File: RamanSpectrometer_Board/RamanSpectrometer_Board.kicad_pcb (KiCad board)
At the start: 2 copper layers, 49.3 x 90.9 mm, 33 parts, among them J1 RJ45_LED_Shielded, Q1 BSS138, Q2 BSS138, Q3 BSS138, Q4 BSS138, Q5 BSS138, U1 Teensy4.1_DEV-16771, U2 OKI 12V-5V, U3 OKI 5V-3V

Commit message: PCB Raman updates
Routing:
- net GND: vias 66 -> 31
- net +12V: vias 0 -> 14

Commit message: PCB Raman again
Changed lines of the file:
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@@
 		(net 4)
 		(net_name "+12V")
-		(layer "F.Cu")
+		(layers "F&B.Cu")
 		(hatch edge 0.5)
 		(priority 2)
-		(connect_pads
+		(connect_pads yes
 			(clearance 0.5)
 		)
 		(min_thickness 0.25)
 		(filled_areas_thickness no)
-		(fill yes
+		(fill
 			(thermal_gap 0.5)
 			(thermal_bridge_width 0.5)
@@
 		(polygon
 			(pts
-				(xy 143.667 53.084) (xy 164.495 53.084) (xy 164.495 123.696) (xy 143.667 123.696)
+				(xy 148.59 53.086) (xy 164.592 53.084) (xy 164.592 123.696) (xy 148.59 123.698)
 			)
 		)
@@
 		(polygon
 			(pts
-				(xy 142.905 43.432) (xy 192.181 43.432) (xy 192.181 134.364) (xy 142.905 134.364)
+				(xy 142.875 43.432) (xy 192.151 43.432) (xy 192.151 134.364) (xy 142.875 134.364)
 			)
 		)
-	)
-	(zone
-		(net 4)
-		(net_name "+12V")
-		(layer "B.Cu")
-		(hatch edge 0.5)
-		(priority 3)
-		(connect_pads
-			(clearance 0.5)
-		)
-		(min_thickness 0.25)
-		(filled_areas_thickness no)
-		(fill yes
-			(thermal_gap 0.5)
-			(thermal_bridge_width 0.5)
-		)
-		(polygon
-			(pts
-				(xy 143.667 53.084) (xy 164.495 53.084) (xy 164.495 123.696) (xy 143.667 123.696)
-			)
-		)
-	)
-	(zone
-		(net 2)
-		(net_name "GND")
-		(layer "B.Cu")
-		(hatch edge 0.5)
-		(priority 1)
-		(connect_pads
-			(clearance 0.5)
-		)
-		(min_thickness 0.25)
-		(filled_areas_thickness no)
-		(fill yes
-			(thermal_gap 0.5)
-			(thermal_bridge_width 0.5)
-		)
-		(polygon
-			(pts
-				(xy 142.905 43.432) (xy 192.181 43.432) (xy 192.181 134.364) (xy 142.905 134.364)
-			)
-		)

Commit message: PCB Raman 12V Plane
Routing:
- removed copper zone on B.Cu, net +12V
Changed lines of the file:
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@@
 		(at 174.244 102.108 90)
 		(property "Reference" "U1"
-			(at 7.108 -4.244 -90)
+			(at -30.48 0 0)
 			(layer "F.SilkS")
 			(effects
@@
 	)
 	(via
-		(at 157.48 106.68)
+		(at 157.48 91.44)
 		(size 0.6)
 		(drill 0.3)
@@
 	)
 	(via
-		(at 157.48 91.44)
+		(at 152.4 81.28)
 		(size 0.6)
 		(drill 0.3)
@@
 	)
 	(via
-		(at 152.4 81.28)
+		(at 152.4 101.6)
 		(size 0.6)
 		(drill 0.3)
@@
 	)
 	(via
-		(at 152.4 101.6)
+		(at 152.4 86.36)
 		(size 0.6)
 		(drill 0.3)
@@
 	)
 	(via
-		(at 152.4 86.36)
+		(at 157.48 106.68)
 		(size 0.6)
 		(drill 0.3)
@@
 		(net 4)
 		(net_name "+12V")
-		(layers "F&B.Cu")
+		(layer "F.Cu")
 		(hatch edge 0.5)
 		(priority 2)
@@
 		(min_thickness 0.25)
 		(filled_areas_thickness no)
-		(fill
+		(fill yes
 			(thermal_gap 0.5)
 			(thermal_bridge_width 0.5)

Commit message: PCB Raman edit and TOF
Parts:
- moved C1 0.35 mm to (168.9, 67.5)
- renumbered D1 to 12V, D3 to 3.3V, D2 to 5V
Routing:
- net +12V: track 0.00 -> 95.0 mm, vias 14 -> 1
- net Red_LED: track 78.0 -> 85.6 mm
- net Green_LED: track 82.7 -> 88.2 mm
- net +3.3V: track 58.2 -> 59.6 mm
- net +3V3: track 24.7 -> 25.8 mm
- net Diode Control: track 87.3 -> 86.3 mm
- net +5V: track 124.1 -> 123.2 mm
- net Net-(C1-Pad1): track 12.8 -> 13.6 mm
- net CCD_ROG_5V: track 11.0 -> 11.6 mm
- net R-: track 68.4 -> 67.9 mm
- net GND: vias 31 -> 39
- removed copper zone on F.Cu, net +12V

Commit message: ihateyoujesse
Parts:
- removed 12V, 3.3V, 5V: Green, LED_SMD:LED_0603_1608Metric_Pad1.05x0.95mm_HandSolder
- removed Q3, Q4: BSS138, Package_TO_SOT_SMD:SOT-23
- removed R10: 33, Resistor_SMD:R_0603_1608Metric_Pad0.98x0.95mm_HandSolder
- removed R8: 78.7, Resistor_SMD:R_0603_1608Metric_Pad0.98x0.95mm_HandSolder
- added D1: Green, LED_SMD:LED_0603_1608Metric_Pad1.05x0.95mm_HandSolder, F.Cu at (150.5, 113.8)
- added D2: Green, LED_SMD:LED_0603_1608Metric_Pad1.05x0.95mm_HandSolder, F.Cu at (150.5, 118.1)
- added D3: Green, LED_SMD:LED_0603_1608Metric_Pad1.05x0.95mm_HandSolder, F.Cu at (150.5, 122.4)
- added U4: VL53L4CX, VL53L4CX:VL53L4CX, F.Cu at (202.7, 94.5)
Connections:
- U1 pad 17: unconnected-(U1-A3-Pad17) -> GPIO
- U1 pad 18: unconnected-(U1-A4-Pad18) -> SDA
- U1 pad 19: unconnected-(U1-A5-Pad19) -> SCL
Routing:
- net Green_LED: track 88.2 -> 0.00 mm
- net Red_LED: track 85.6 -> 0.00 mm
- net +12V: track 95.0 -> 57.2 mm, vias 1 -> 2
- net SDA: vias 0 -> 1
- net GND: vias 39 -> 34

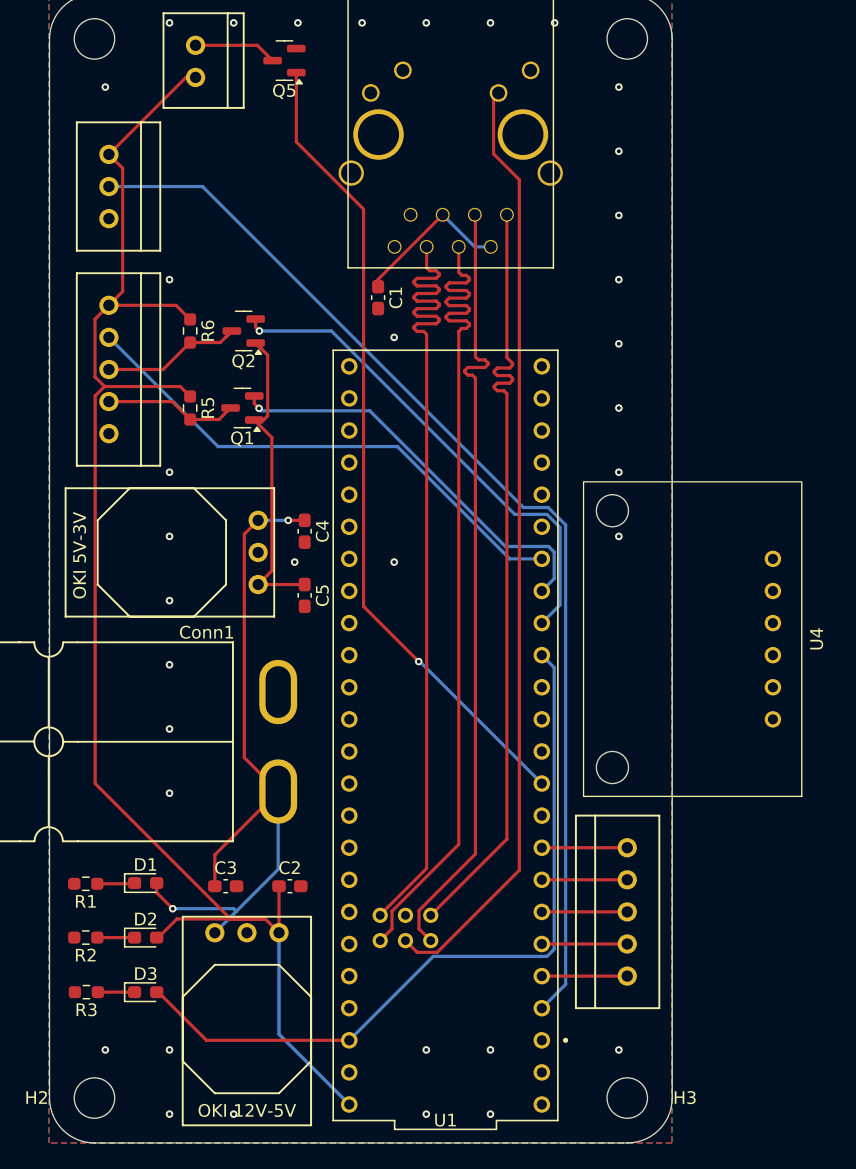
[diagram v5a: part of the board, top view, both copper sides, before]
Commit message: Raman PCB Additions
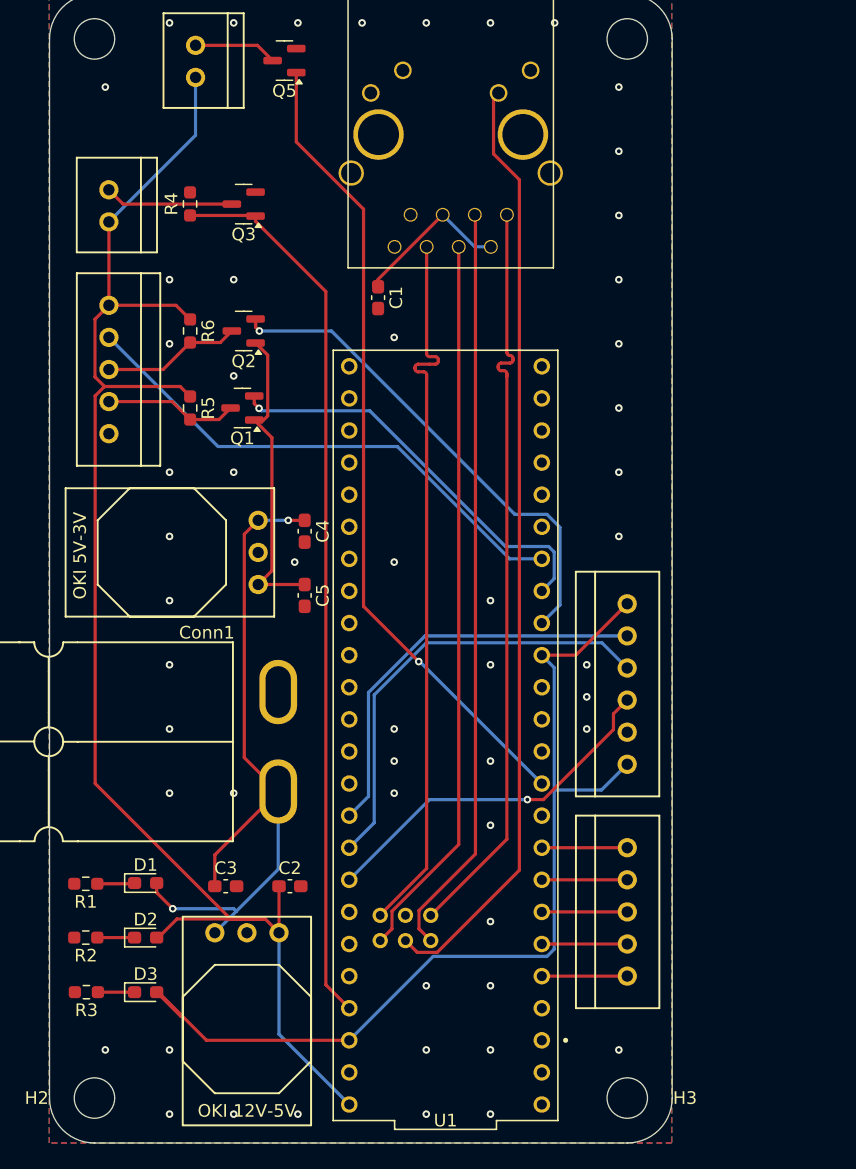
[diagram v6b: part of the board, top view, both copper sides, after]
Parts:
- removed Conn3: Diode, MRDT_Connectors:MOLEX_SL_03_Vertical
- removed U4: VL53L4CX, VL53L4CX:VL53L4CX
- added Conn6: Laser, MRDT_Connectors:MOLEX_SL_02_Vertical, F.Cu at (147.6, 58.9)
- added Conn7: TOF Sensor, MRDT_Connectors:MOLEX_SL_06_Vertical, F.Cu at (192.6, 98.2)
- added Q3: BSS138, Package_TO_SOT_SMD:SOT-23, F.Cu at (158.3, 60.1)
- added R4: 4.7k, Resistor_SMD:R_0603_1608Metric_Pad0.98x0.95mm_HandSolder, F.Cu at (154.0, 60.0)
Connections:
- U1 pad 23: unconnected-(U1-A9-Pad23) -> Green_Laser_3V3
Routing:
- net Diode Control: track 86.3 -> 0.00 mm
- net Green_Laser_3V3: track 0.00 -> 71.0 mm
- net SDA: track 0.00 -> 35.7 mm, vias 1 -> 0
- net GPIO: track 0.00 -> 32.7 mm
- net SCL: track 0.00 -> 28.6 mm, vias 0 -> 1
- net +3.3V: track 59.6 -> 77.5 mm
- net R+: track 68.0 -> 57.5 mm
- net R-: track 67.9 -> 57.4 mm
- net Net-(Q3-D): track 0.00 -> 10.2 mm
- net T-: track 62.6 -> 59.7 mm
- net T+: track 62.4 -> 59.6 mm
- net +12V: track 57.2 -> 59.1 mm
- net +5V: track 123.2 -> 122.0 mm
- net +3V3: track 25.8 -> 25.1 mm
- net CCD_ROG_5V: track 11.6 -> 11.0 mm
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
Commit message: Raman PCB Final
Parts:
- added G***: LOGO, MRDT_Silkscreens:0_MRDT_Logo_7.5mm, F.Cu at (187.7, 74.2)
- added G***: LOGO, LOGO, F.Cu at (188.5, 82.7)
- added G***: LOGO, LOGO, B.Cu at (168.7, 88.9)
- renumbered D1 to 12V, D3 to 3.3V, D2 to 5V
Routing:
- net +5V: track 122.0 -> 123.8 mm
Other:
- board text added: "AndersonPP"
- board text added: "CCD"
- board text added: "Fan"
- board text added: "Gantry"
- board text added: "Laser"
- board text added: "OKI 12V-5V"
- board text added: "OKI 5V-3V"
- board text added: "Raman Spectrometer, Rev 1 Mars Rover, 2025 Missouri S&T Zen Thurman & Noah S"
- board text added: "TOF"

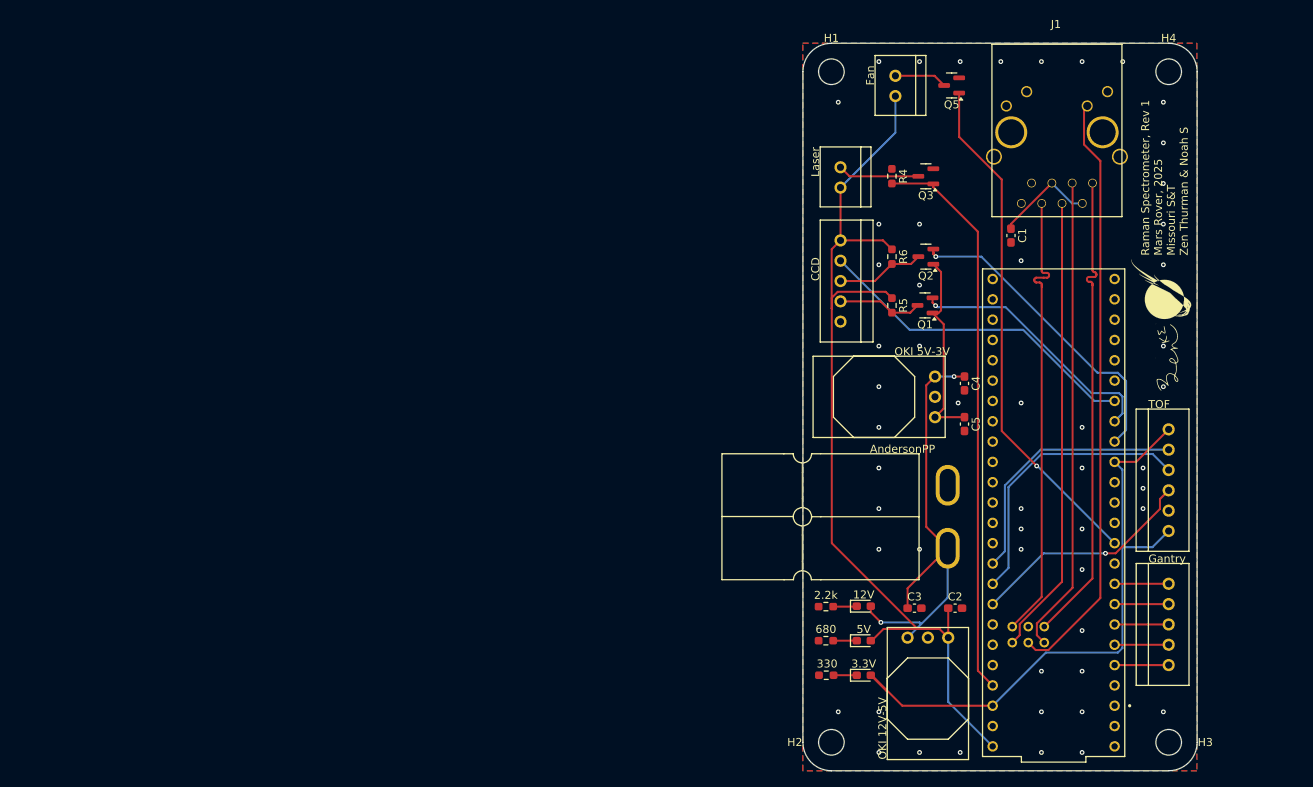
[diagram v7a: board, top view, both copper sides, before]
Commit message: Raman PCB board review pt.1
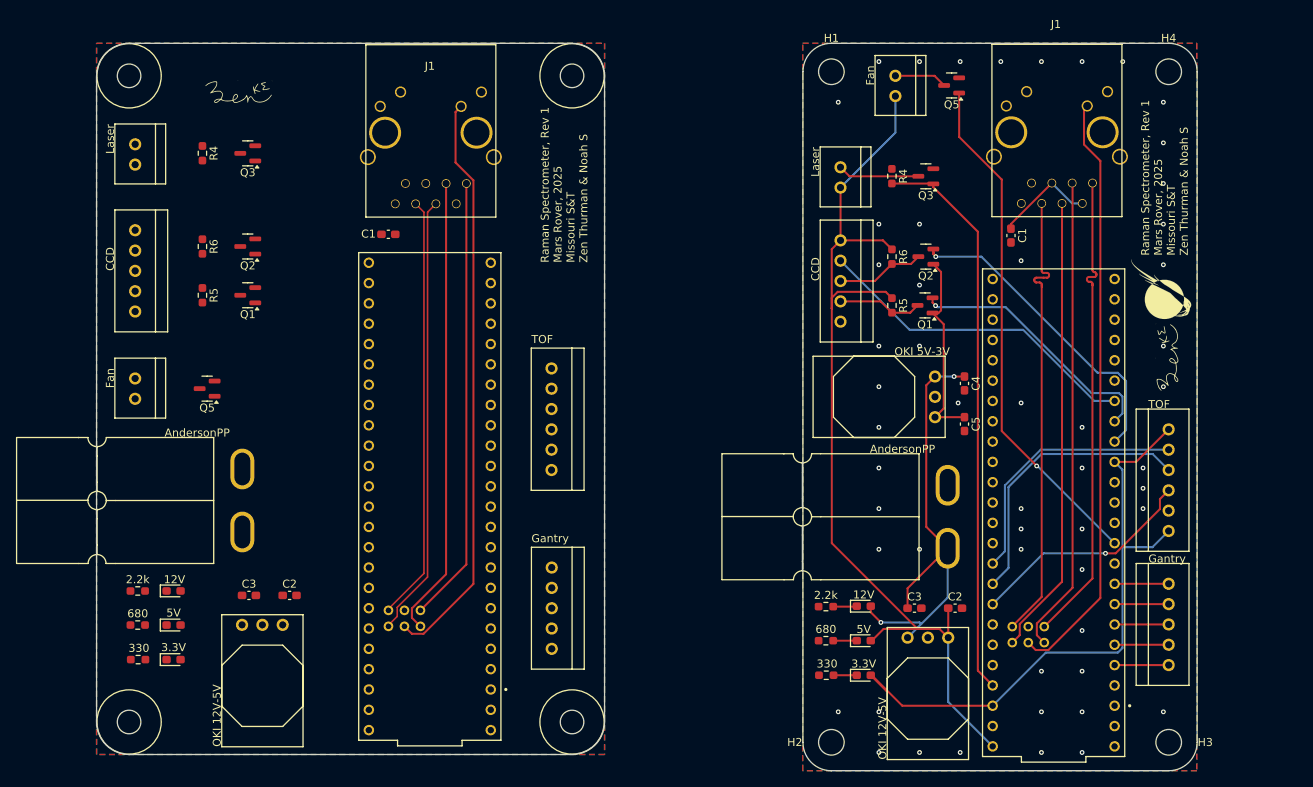
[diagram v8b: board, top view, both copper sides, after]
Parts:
- added C1: 0.1uF, Capacitor_SMD:C_0603_1608Metric_Pad1.08x0.95mm_HandSolder, F.Cu at (91.1, 67.3)
- added C2: 10uF, Capacitor_SMD:C_0603_1608Metric_Pad1.08x0.95mm_HandSolder, F.Cu at (78.7, 112.4)
- added C3: 10uF, Capacitor_SMD:C_0603_1608Metric_Pad1.08x0.95mm_HandSolder, F.Cu at (73.7, 112.4)
- added Conn1: AndersonPP, MRDT_Connectors:Square_Anderson_2_H_Side_By_Side_PV, F.Cu at (73.0, 96.3)
- added Conn2: Gantry, MRDT_Connectors:MOLEX_SL_05_Vertical, F.Cu at (111.5, 109.0)
- added Conn4: CCD, MRDT_Connectors:MOLEX_SL_05_Vertical, F.Cu at (59.4, 66.8)
- added Conn5: Fan, MRDT_Connectors:MOLEX_SL_02_Vertical, F.Cu at (59.4, 85.3)
- added Conn6: Laser, MRDT_Connectors:MOLEX_SL_02_Vertical, F.Cu at (59.4, 56.1)
- added Conn7: TOF Sensor, MRDT_Connectors:MOLEX_SL_06_Vertical, F.Cu at (107.5, 90.3)
- added D1: 12V, LED_SMD:LED_0603_1608Metric_Pad1.05x0.95mm_HandSolder, F.Cu at (64.2, 111.9)
- added D2: 5V, LED_SMD:LED_0603_1608Metric_Pad1.05x0.95mm_HandSolder, F.Cu at (64.2, 116.2)
- added D3: 3.3V, LED_SMD:LED_0603_1608Metric_Pad1.05x0.95mm_HandSolder, F.Cu at (64.2, 120.5)
- added G***: LOGO, LOGO, F.Cu at (72.4, 49.5)
- added G***: LOGO, LOGO, B.Cu at (87.1, 90.4)
- added H1: ~, MRDT_Drill_Holes:4_40_Hole, F.Cu at (58.7, 47.5)
- added H2: ~, MRDT_Drill_Holes:4_40_Hole, F.Cu at (58.7, 128.3)
- added H3: ~, MRDT_Drill_Holes:4_40_Hole, F.Cu at (114.0, 128.3)
- added H4: ~, MRDT_Drill_Holes:4_40_Hole, F.Cu at (114.0, 47.5)
- added J1: RJ45_LED_Shielded, MRDT_Connectors:RJ45_Teensy, F.Cu at (96.3, 41.6)
- added Q1: BSS138, Package_TO_SOT_SMD:SOT-23, F.Cu at (73.5, 74.9)
- added Q2: BSS138, Package_TO_SOT_SMD:SOT-23, F.Cu at (73.5, 68.8)
- added Q3: BSS138, Package_TO_SOT_SMD:SOT-23, F.Cu at (73.5, 57.2)
- added Q5: BSS138, Package_TO_SOT_SMD:SOT-23, F.Cu at (68.4, 86.6)
- added R1: 2.2k, Resistor_SMD:R_0603_1608Metric_Pad0.98x0.95mm_HandSolder, F.Cu at (59.8, 111.9)
- added R2: 680, Resistor_SMD:R_0603_1608Metric_Pad0.98x0.95mm_HandSolder, F.Cu at (59.8, 116.2)
- added R3: 330, Resistor_SMD:R_0603_1608Metric_Pad0.98x0.95mm_HandSolder, F.Cu at (59.8, 120.5)
- added R4: 4.7k, Resistor_SMD:R_0603_1608Metric_Pad0.98x0.95mm_HandSolder, F.Cu at (67.8, 57.2)
- added R5: 4.7k, Resistor_SMD:R_0603_1608Metric_Pad0.98x0.95mm_HandSolder, F.Cu at (67.8, 74.9)
- added R6: 4.7k, Resistor_SMD:R_0603_1608Metric_Pad0.98x0.95mm_HandSolder, F.Cu at (67.8, 68.8)
- added U1: Teensy4.1_DEV-16771, MRDT_Shields:Teensy_4_1_Ethernet, F.Cu at (96.3, 100.1)
- added U2: OKI 12V-5V, MRDT_Devices:OKI_Horizontal, F.Cu at (72.8, 116.1)
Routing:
- net LED: track 74.6 -> 147.1 mm
- net T-: track 59.7 -> 117.3 mm
- net T+: track 59.6 -> 115.4 mm
- net R+: track 57.5 -> 112.7 mm
- net R-: track 57.4 -> 110.5 mm
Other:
- board size 49.3 x 90.9 mm -> 137.6 x 90.9 mm
